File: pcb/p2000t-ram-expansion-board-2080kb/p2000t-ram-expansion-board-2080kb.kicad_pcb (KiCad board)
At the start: 2 copper layers, 108.6 x 66.8 mm, 30 parts, among them J1 EXPANSION BOARD, J2 POWER, J3 TERMINAL, U1 74HC04, U10 AS6C4008-55PCN, U11 AS6C4008-55PCN, U12 74HC138, U13 74HC74, U2 AS6C4008-55PCN, U3 74HC00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

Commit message: Adding gerbers
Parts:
- added C14: 0.1uF, Capacitor_THT:C_Disc_D5.0mm_W2.5mm_P5.00mm, F.Cu at (212.9, 74.3)
- added REF**: OSHW-Logo2_14.6x12mm_SilkScreen, Symbol:OSHW-Logo2_14.6x12mm_SilkScreen, F.Cu at (228.8, 127.1)
- moved C7 139.2 mm to (110.7, 71.8)
- moved U13 137.9 mm to (218.0, 103.6), turned to 90 degrees
- moved U12 109.5 mm to (185.6, 80.7), turned to 90 degrees
- moved C4 106.9 mm to (135.4, 71.8)
- moved C1 103.5 mm to (160.2, 77.2)
- moved U4 103.5 mm to (150.1, 82.0)
- moved C3 101.1 mm to (139.5, 126.7)
- moved J1 96.2 mm to (208.8, 127.3)
- moved C13 90.3 mm to (175.5, 108.7), turned to -90 degrees
- moved C11 87.3 mm to (180.5, 74.4), turned to -90 degrees
- moved C12 83.7 mm to (175.5, 85.8), turned to -90 degrees
- moved C9 60.3 mm to (175.5, 97.2), turned to -90 degrees
- moved U6 49.4 mm to (218.0, 80.7), turned to 90 degrees
- moved C8 49.2 mm to (212.9, 108.7), turned to -90 degrees
- moved C2 49.1 mm to (212.9, 85.8), turned to -90 degrees
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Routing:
- net GND: track 0.00 -> 1093.0 mm
- net +5V: track 0.00 -> 855.0 mm
- net A0: track 0.00 -> 263.6 mm, vias 0 -> 3
- net ~{RD}: track 0.00 -> 253.2 mm, vias 0 -> 2
- net D7: track 0.00 -> 249.7 mm, vias 0 -> 1
- net D1: track 0.00 -> 248.1 mm, vias 0 -> 3
- net D6: track 0.00 -> 234.6 mm, vias 0 -> 2
- net D0: track 0.00 -> 229.4 mm, vias 0 -> 3
- net ~{WR}: track 0.00 -> 224.8 mm, vias 0 -> 3
- net D2: track 0.00 -> 215.3 mm, vias 0 -> 2
- net A4: track 0.00 -> 202.4 mm
- net A7: track 0.00 -> 200.1 mm
- net A6: track 0.00 -> 200.1 mm
- net D4: track 0.00 -> 199.2 mm
- net A3: track 0.00 -> 193.3 mm
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- added copper zone on B.Cu, net +5V
- added copper zone on F.Cu, net GND
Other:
- board size 108.6 x 66.8 mm -> 203.7 x 67.7 mm
- board text added: "0xE000-0xFFFF (64 banks x 8kb; 0x00-0x3F)"
- board text added: "0xE000-0xFFFF (64 banks x 8kb; 0x40-0x7F)"
- board text added: "0xE000-0xFFFF (64 banks x 8kb; 0x80-0xBF)"
- board text added: "0xE000-0xFFFF (64 banks x 8kb; 0xC0-0xFF)"
- board text removed: "0xE000-0xFFFF (64 banks x 8kb)"

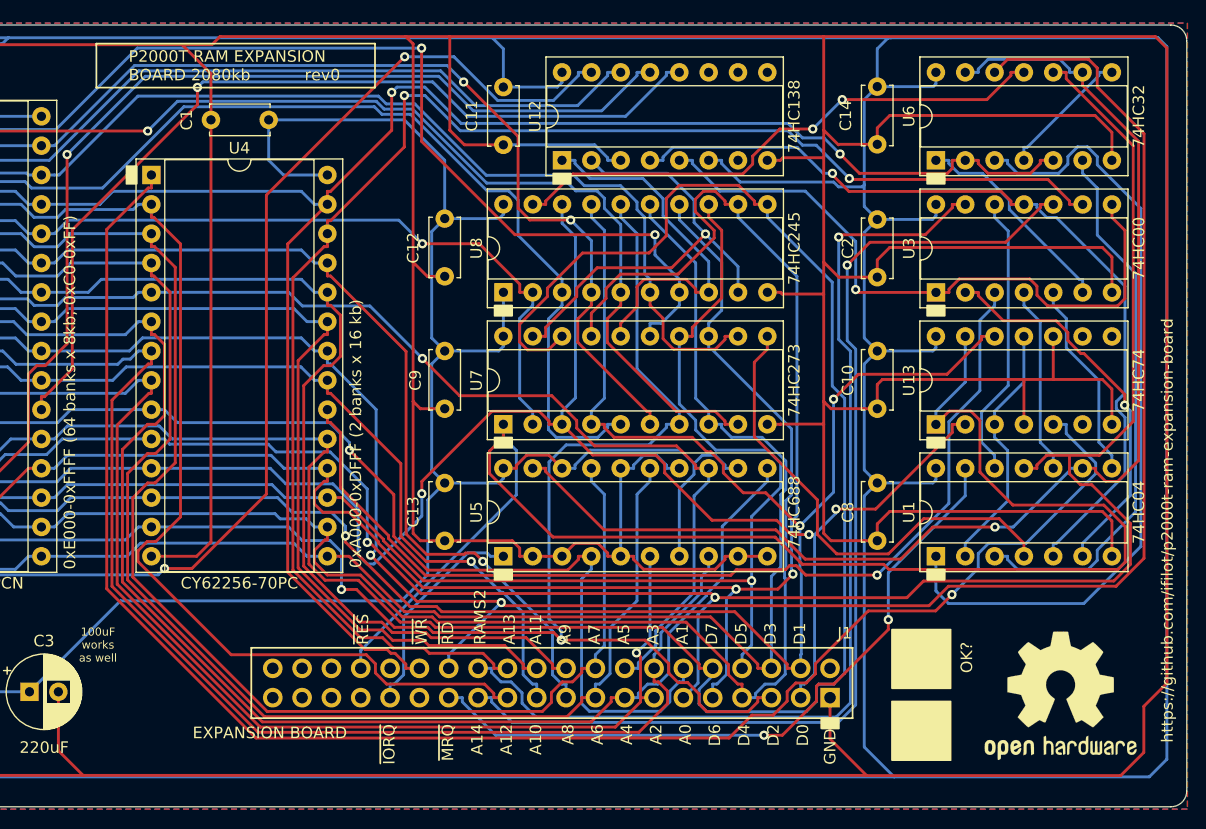
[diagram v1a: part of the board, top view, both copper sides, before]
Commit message: Fixing bug in wiring
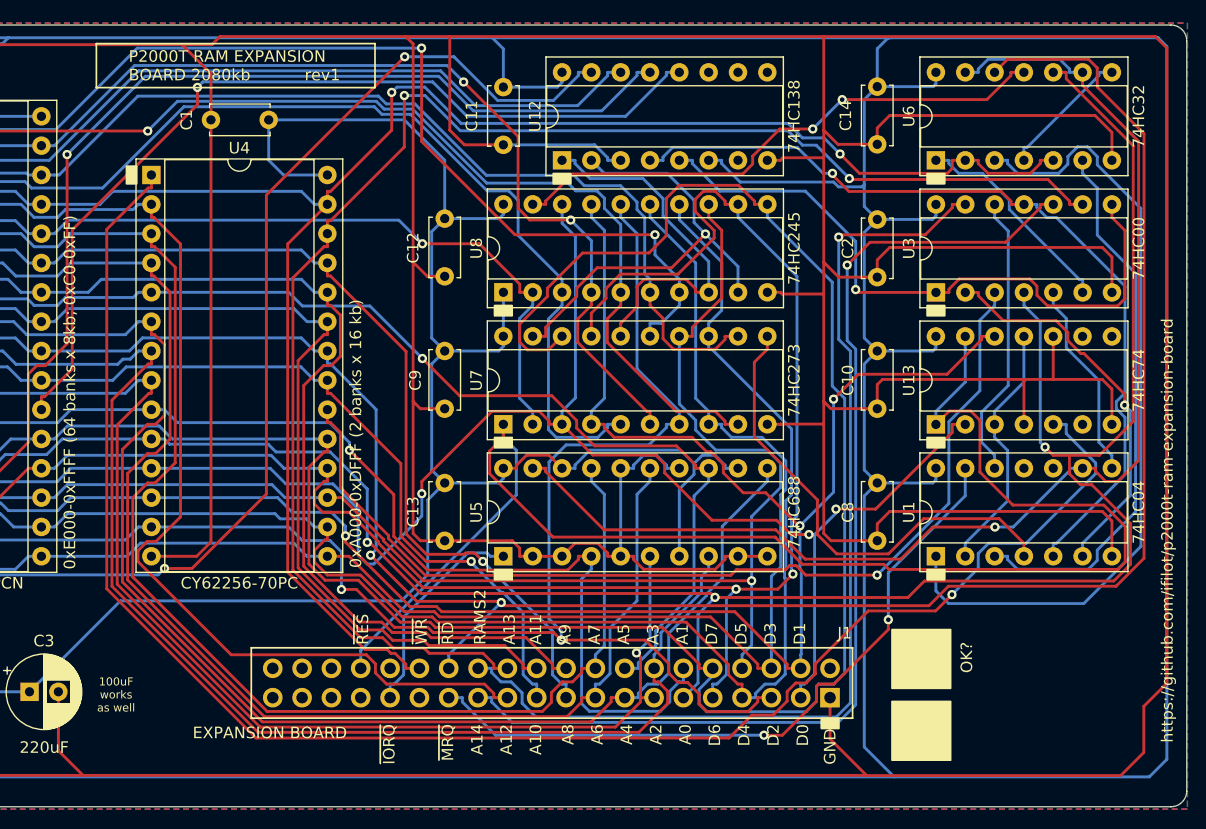
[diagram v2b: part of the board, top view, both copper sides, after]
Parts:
- removed REF**: OSHW-Logo2_14.6x12mm_SilkScreen, Symbol:OSHW-Logo2_14.6x12mm_SilkScreen
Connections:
- U1 pad 10: Net-(U1-Pad10) -> unconnected-(U1-Pad10)
- U1 pad 11: A0 -> GND
- U3 pad 4: Net-(U1-Pad10) -> A0
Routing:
- net Net-(U1-Pad10): track 16.3 -> 0.00 mm
- net A0: track 263.6 -> 275.6 mm, vias 3 -> 4
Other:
- board text added: "rev1"
- board text removed: "rev0"

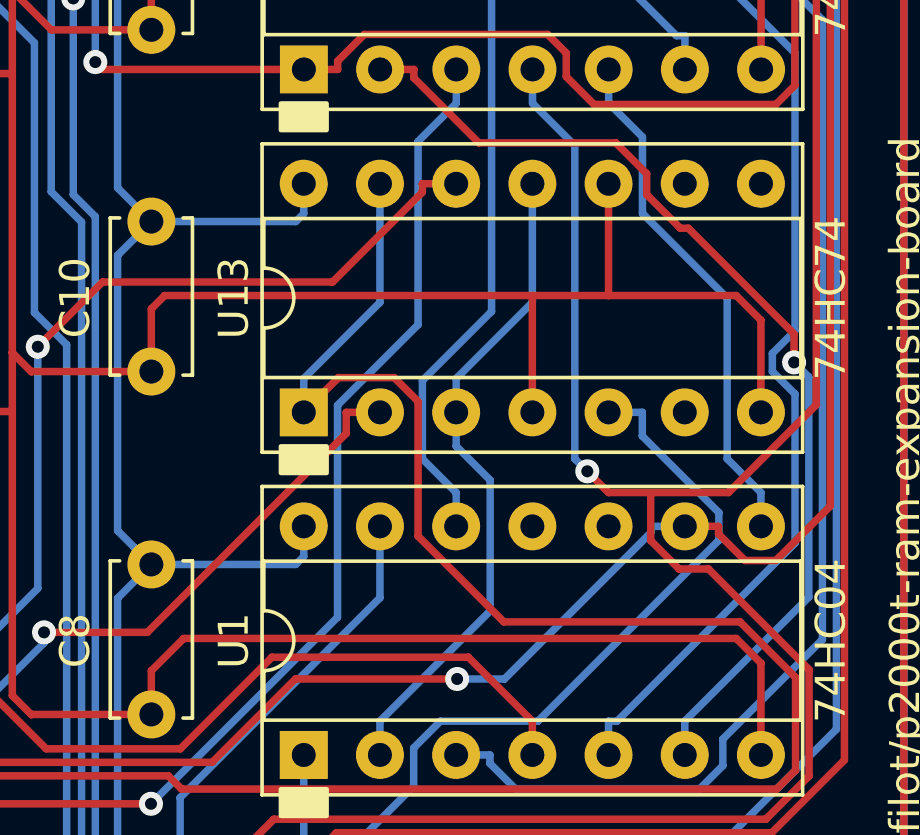
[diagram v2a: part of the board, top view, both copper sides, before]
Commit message: Fixing another bug 74HC74
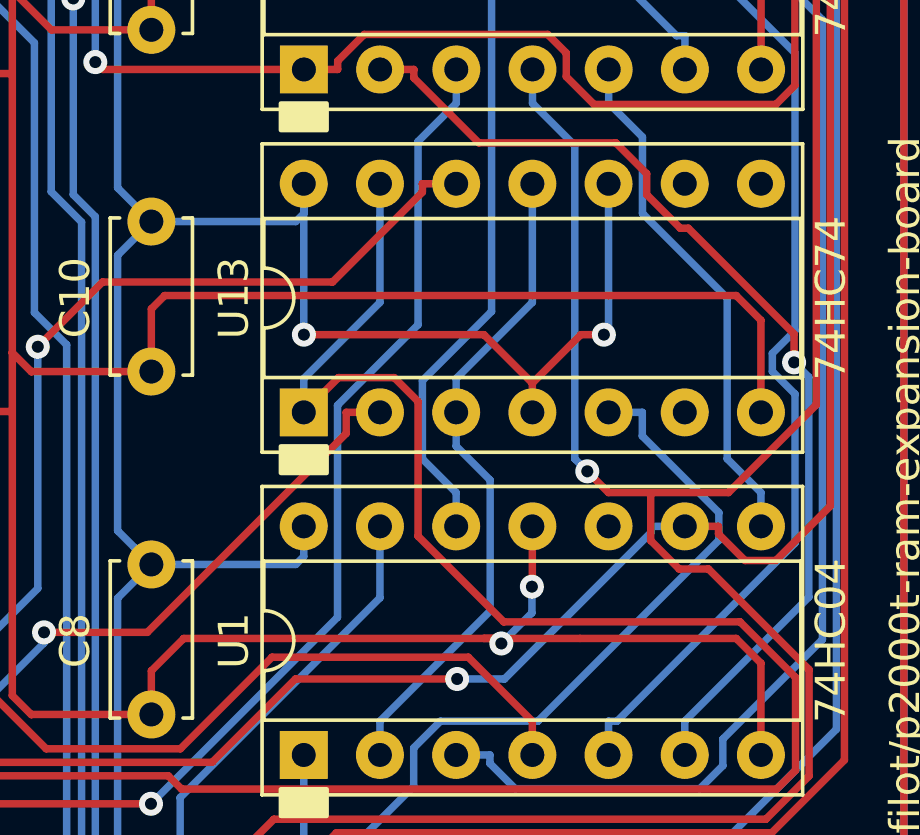
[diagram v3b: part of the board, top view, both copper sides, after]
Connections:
- U13 pad 10: GND -> +5V
- U13 pad 4: GND -> +5V
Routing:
- net +5V: track 855.0 -> 877.5 mm, vias 0 -> 2
- net GND: track 1093.0 -> 1090.4 mm, vias 0 -> 2
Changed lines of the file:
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@@
       (net 51 "Net-(U13A-C)") (pinfunction "C") (pintype "input"))
     (pad "4" thru_hole oval (at 0 7.62 90) (size 1.6 1.6) (drill 0.8) (layers "*.Cu" "*.Mask")
-      (net 39 "GND") (pinfunction "~{S}") (pintype "input"))
+      (net 43 "+5V") (pinfunction "~{S}") (pintype "input"))
     (pad "5" thru_hole oval (at 0 10.16 90) (size 1.6 1.6) (drill 0.8) (layers "*.Cu" "*.Mask")
       (net 68 "RAMS0") (pinfunction "Q") (pintype "output"))
@@
       (net 77 "unconnected-(U13B-Q-Pad9)") (pinfunction "Q") (pintype "output+no_connect"))
     (pad "10" thru_hole oval (at 7.62 10.16 90) (size 1.6 1.6) (drill 0.8) (layers "*.Cu" "*.Mask")
-      (net 39 "GND") (pinfunction "~{S}") (pintype "input"))
+      (net 43 "+5V") (pinfunction "~{S}") (pintype "input"))
     (pad "11" thru_hole oval (at 7.62 7.62 90) (size 1.6 1.6) (drill 0.8) (layers "*.Cu" "*.Mask")
       (net 51 "Net-(U13A-C)") (pinfunction "C") (pintype "input"))
@@
   (segment (start 155.215 77.2136) (end 155.215 113.771) (width 0.25) (layer "F.Cu") (net 39))
   (segment (start 45.1712 71.8288) (end 57.4358 71.8288) (width 0.25) (layer "F.Cu") (net 39))
-  (segment (start 225.615 99.695) (end 225.615 103.5888) (width 0.25) (layer "F.Cu") (net 39))
+  (segment (start 224.413346 111.125) (end 224.581496 111.29315) (width 0.25) (layer "F.Cu") (net 39))
   (segment (start 233.235 103.5888) (end 233.235 103.589) (width 0.25) (layer "F.Cu") (net 39))
   (segment (start 208.28 80.4935) (end 204.7456 80.4935) (width 0.25) (layer "F.Cu") (net 39))
   (segment (start 212.915 100.14) (end 213.36 99.695) (width 0.25) (layer "F.Cu") (net 39))
   (segment (start 208.826 130.826) (end 208.826 127.252) (width 0.25) (layer "F.Cu") (net 39))
-  (segment (start 228.155 95.9688) (end 228.155 99.695) (width 0.25) (layer "F.Cu") (net 39))
   (segment (start 153.977 115.009) (end 150.0552 115.009) (width 0.25) (layer "F.Cu") (net 39))
   (segment (start 172.72 89.535) (end 172.72 101.6) (width 0.25) (layer "F.Cu") (net 39))
@@
   (segment (start 208.28 78.105) (end 209.55 79.375) (width 0.25) (layer "F.Cu") (net 39))
   (segment (start 212.915 102.2288) (end 212.915 100.14) (width 0.25) (layer "F.Cu") (net 39))
+  (segment (start 224 111.125) (end 227.2 111.125) (width 0.25) (layer "F.Cu") (net 39))
+  (segment (start 213.995 111.125) (end 224 111.125) (width 0.25) (layer "F.Cu") (net 39))
   (segment (start 213.995 76.835) (end 231.775 76.835) (width 0.25) (layer "F.Cu") (net 39))
   (segment (start 38.735 117.475) (end 38.1 116.84) (width 0.25) (layer "F.Cu") (net 39))
+  (segment (start 225.615 107.3888) (end 225.615 109.385) (width 0.25) (layer "F.Cu") (net 39))
   (segment (start 232.41 99.695) (end 233.235 100.52) (width 0.25) (layer "F.Cu") (net 39))
   (segment (start 82.68 70.7038) (end 104.56 70.7038) (width 0.25) (layer "F.Cu") (net 39))
@@
   (segment (start 189.5697 114.7274) (end 189.5697 115.0088) (width 0.25) (layer "F.Cu") (net 39))
   (segment (start 44.4738 72) (end 45 72) (width 0.25) (layer "F.Cu") (net 39))
+  (segment (start 225.615 109.385) (end 225.6 109.4) (width 0.25) (layer "F.Cu") (net 39))
   (segment (start 52.2602 115.009) (end 52.26 115.009) (width 0.25) (layer "F.Cu") (net 39))
   (segment (start 104.648 115.062) (end 104.595 115.009) (width 0.25) (layer "F.Cu") (net 39))
@@
   (segment (start 208.28 101.6) (end 208.28 103.5604) (width 0.25) (layer "F.Cu") (net 39))
   (segment (start 211.985 133.985) (end 144.145 133.985) (width 0.25) (layer "F.Cu") (net 39))
-  (segment (start 213.995 111.125) (end 232.41 111.125) (width 0.25) (layer "F.Cu") (net 39))
   (segment (start 81.555 71.8288) (end 81.555 114.279) (width 0.25) (layer "F.Cu") (net 39))
   (segment (start 132.715 132.715) (end 132.715 119.38) (width 0.25) (layer "F.Cu") (net 39))
@@
   (segment (start 130.81 117.475) (end 90.805 117.475) (width 0.25) (layer "F.Cu") (net 39))
   (segment (start 200.855 115.0088) (end 199.7297 115.0088) (width 0.25) (layer "F.Cu") (net 39))
+  (segment (start 227.2 111.125) (end 232.41 111.125) (width 0.25) (layer "F.Cu") (net 39))
   (segment (start 130.45 71.8288) (end 130.45 113.39) (width 0.25) (layer "F.Cu") (net 39))
   (segment (start 57.4358 71.8288) (end 57.4358 114.014) (width 0.25) (layer "F.Cu") (net 39))
@@
   (segment (start 76.3952 115.009) (end 76.395 115.009) (width 0.25) (layer "F.Cu") (net 39))
   (segment (start 81.555 71.8288) (end 82.68 70.7038) (width 0.25) (layer "F.Cu") (net 39))
+  (segment (start 224 111.125) (end 224.413346 111.125) (width 0.25) (layer "F.Cu") (net 39))
   (segment (start 130.45 71.8288) (end 131.575 70.7038) (width 0.25) (layer "F.Cu") (net 39))
   (segment (start 208.28 92.2968) (end 208.28 101.6) (width 0.25) (layer "F.Cu") (net 39))
@@
   (segment (start 133.985 133.985) (end 132.715 132.715) (width 0.25) (layer "F.Cu") (net 39))
   (segment (start 90.805 117.475) (end 90.17 117.475) (width 0.25) (layer "F.Cu") (net 39))
+  (via (at 224.581496 111.29315) (size 0.8) (drill 0.4) (layers "F.Cu" "B.Cu") (net 39))
+  (via (at 225.6 109.4) (size 0.8) (drill 0.4) (layers "F.Cu" "B.Cu") (net 39))
   (segment (start 190.695 80.7188) (end 189.5697 80.7188) (width 0.25) (layer "B.Cu") (net 39))
   (segment (start 195.775 107.3888) (end 194.6497 107.3888) (width 0.25) (layer "B.Cu") (net 39))
+  (segment (start 225.6 110.274646) (end 224.581496 111.29315) (width 0.25) (layer "B.Cu") (net 39))
   (segment (start 191.8203 107.1074) (end 191.8203 107.3888) (width 0.25) (layer "B.Cu") (net 39))
   (segment (start 190.695 107.3888) (end 191.2577 107.3888) (width 0.25) (layer "B.Cu") (net 39))
@@
   (segment (start 193.8058 106.2635) (end 192.6642 106.2635) (width 0.25) (layer "B.Cu") (net 39))
   (segment (start 190.695 115.0088) (end 190.695 113.8835) (width 0.25) (layer "B.Cu") (net 39))
+  (segment (start 225.6 109.4) (end 225.6 110.274646) (width 0.25) (layer "B.Cu") (net 39))
   (segment (start 192.6642 106.2635) (end 191.8203 107.1074) (width 0.25) (layer "B.Cu") (net 39))
   (segment (start 191.2577 107.3888) (end 191.8203 107.3888) (width 0.25) (layer "B.Cu") (net 39))
@@
   (segment (start 112.8776 80.5741) (end 93.8856 80.5741) (width 0.25) (layer "B.Cu") (net 41))
   (segment (start 180.535 107.3888) (end 181.6603 107.3888) (width 0.25) (layer "F.Cu") (net 43))
+  (segment (start 225.615 102.615) (end 225.615 103.5888) (width 0.25) (layer "F.Cu") (net 43))
+  (segment (start 218 101) (end 224 101) (width 0.25) (layer "F.Cu") (net 43))
   (segment (start 181.6603 107.3888) (end 181.6603 107.1408) (width 0.25) (layer "F.Cu") (net 43))
   (segment (start 184.479 106.2528) (end 185.615 107.3888) (width 0.25) (layer "F.Cu") (net 43))
+  (segment (start 228 101) (end 227.23 101) (width 0.25) (layer "F.Cu") (net 43))
+  (segment (start 224 101) (end 225.615 102.615) (width 0.25) (layer "F.Cu") (net 43))
   (segment (start 182.5483 106.2528) (end 184.479 106.2528) (width 0.25) (layer "F.Cu") (net 43))
+  (segment (start 227.23 101) (end 225.615 102.615) (width 0.25) (layer "F.Cu") (net 43))
   (segment (start 181.6603 107.1408) (end 182.5483 106.2528) (width 0.25) (layer "F.Cu") (net 43))
+  (via (at 228 101) (size 0.8) (drill 0.4) (layers "F.Cu" "B.Cu") (net 43))
+  (via (at 218 101) (size 0.8) (drill 0.4) (layers "F.Cu" "B.Cu") (net 43))
   (segment (start 217.765 74.335) (end 217.995 74.105) (width 0.25) (layer "B.Cu") (net 43))
   (segment (start 180.54 92.1488) (end 180.54 93.2741) (width 0.25) (layer "B.Cu") (net 43))
@@
   (segment (start 174.33 86.89) (end 174.33 96.1038) (width 0.25) (layer "B.Cu") (net 43))
   (segment (start 197.7614 106.2635) (end 198.8858 106.2635) (width 0.25) (layer "B.Cu") (net 43))
+  (segment (start 228.155 100.845) (end 228 101) (width 0.25) (layer "B.Cu") (net 43))
   (segment (start 217.731 108.659) (end 217.995 108.395) (width 0.25) (layer "B.Cu") (net 43))
   (segment (start 40.386 70.104) (end 37.846 72.644) (width 0.25) (layer "B.Cu") (net 43))
@@
   (segment (start 180.139 97.2288) (end 180.535 96.833) (width 0.25) (layer "B.Cu") (net 43))
   (segment (start 195.8782 105.8131) (end 197.045 106.9799) (width 0.25) (layer "B.Cu") (net 43))
+  (segment (start 217.995 100.995) (end 218 101) (width 0.25) (layer "B.Cu") (net 43))
   (segment (start 88.2798 70.104) (end 86.555 71.8288) (width 0.25) (layer "B.Cu") (net 43))
   (segment (start 110.685 71.8288) (end 110.685 75.633) (width 0.25) (layer "B.Cu") (net 43))
@@
   (segment (start 139.5002 126.7438) (end 147.372 118.872) (width 0.25) (layer "B.Cu") (net 43))
   (segment (start 195.775 115.0088) (end 195.775 109.189) (width 0.25) (layer "B.Cu") (net 43))
+  (segment (start 228.155 95.9688) (end 228.155 100.845) (width 0.25) (layer "B.Cu") (net 43))
   (segment (start 213.868 70.104) (end 212.915 71.057) (width 0.25) (layer "B.Cu") (net 43))
   (segment (start 37.846 105.156) (end 38.862 106.172) (width 0.25) (layer "B.Cu") (net 43))
@@
   (segment (start 180.535 71.061) (end 180.535 74.375) (width 0.25) (layer "B.Cu") (net 43))
   (segment (start 38.862 106.172) (end 38.9152 106.119) (width 0.25) (layer "B.Cu") (net 43))
+  (segment (start 217.995 95.9688) (end 217.995 100.995) (width 0.25) (layer "B.Cu") (net 43))
   (segment (start 63.4468 76.9088) (end 67.5 76.9088) (width 0.25) (layer "B.Cu") (net 43))
   (segment (start 218 85.53) (end 218 84.5388) (width 0.25) (layer "B.Cu") (net 43))

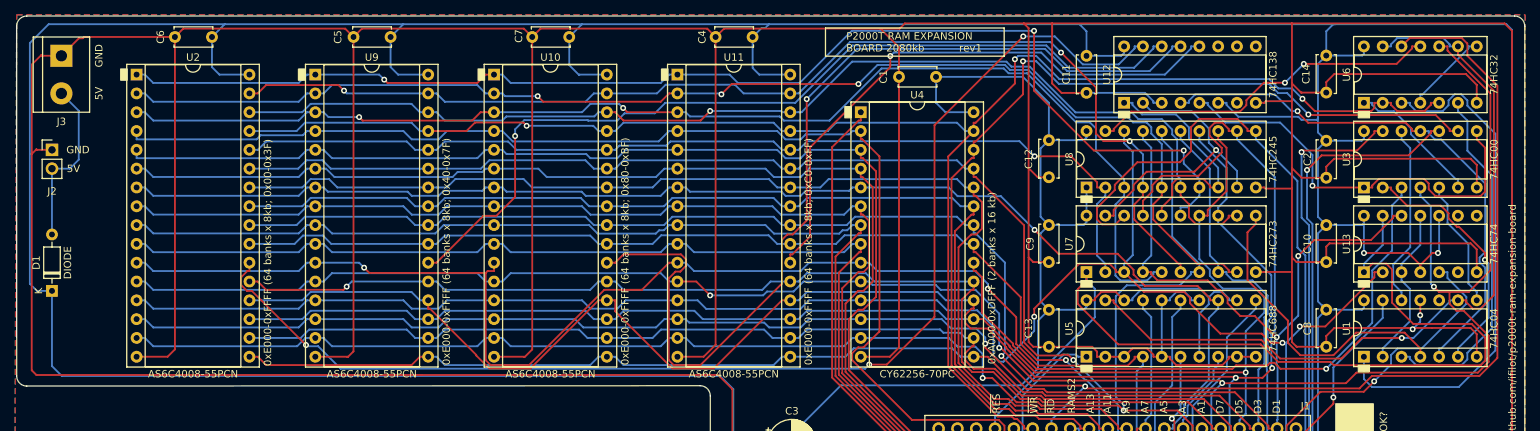
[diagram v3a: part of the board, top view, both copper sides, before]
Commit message: Changing size
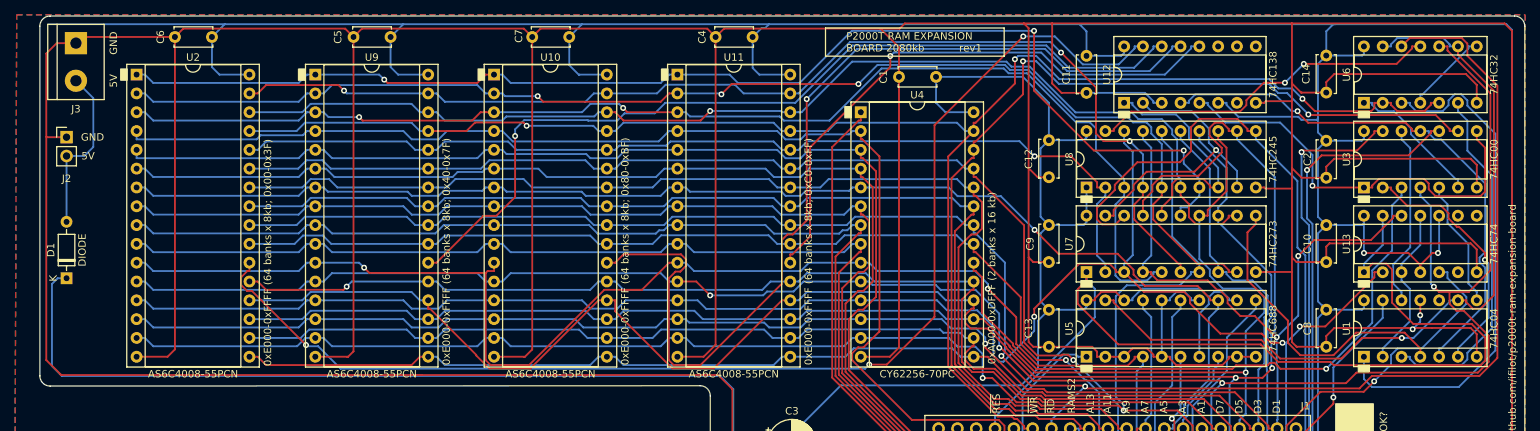
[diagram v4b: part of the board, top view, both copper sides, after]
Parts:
- moved J3 2.60 mm to (44.1, 72.7)
- moved D1 2.60 mm to (42.8, 104.4)
- moved J2 2.60 mm to (42.8, 85.4)
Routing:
- net +5V: track 877.5 -> 841.2 mm
- net GND: track 1090.4 -> 1086.3 mm
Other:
- board size 203.7 x 67.7 mm -> 200.5 x 67.7 mm

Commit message: Revising PCBs
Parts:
- added LOGO1: OSHW-Logo2_14.6x12mm_Copper, Symbol:OSHW-Logo2_14.6x12mm_Copper, F.Cu at (227.5, 127.0)
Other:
- board text added: "rev2"
- board text removed: "rev1"
